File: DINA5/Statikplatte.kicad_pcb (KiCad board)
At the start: 2 copper layers, 100 x 100 mm, 32 parts, among them J1 VIN, J10 HV, J2 GND, J3 GND, J4 GND, J5 GND, J6 GND, J7 HV, J8 HV, J9 HV

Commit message: added DINA5 files
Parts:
- removed G***: LOGO, otter:otter_small1
- J1, J10, J2, J3, J4, J5, J6, J7, J8, J9: footprint TestPoint:TestPoint_Pad_2.5x2.5mm -> otter:Pads7.5x12
- moved J10 81.0 mm to (21.0, 104.0)
- moved J6 81.0 mm to (21.0, 74.0)
- moved J5 42.6 mm to (105.0, 21.0), turned to 270 degrees
- moved J8 42.6 mm to (135.0, 21.0), turned to 90 degrees
- moved J1 36.7 mm to (79.0, 83.0)
- moved J3 35.7 mm to (79.0, 95.0)
- moved C6 32.0 mm to (119.9, 95.0)
- moved C1 32.0 mm to (90.0, 83.0)
- moved C10 32.0 mm to (143.9, 95.0)
- moved C2 32.0 mm to (96.0, 95.0)
- moved C3 32.0 mm to (102.0, 83.0)
- moved C4 32.0 mm to (108.0, 95.0)
- moved C5 32.0 mm to (114.0, 83.0)
- moved C7 32.0 mm to (126.0, 83.0)
- moved C8 32.0 mm to (132.0, 95.0)
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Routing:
- net /GND: track 209.7 -> 312.2 mm
- net /HV: track 188.9 -> 267.2 mm
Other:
- board size 100 x 100 mm -> 210 x 148 mm

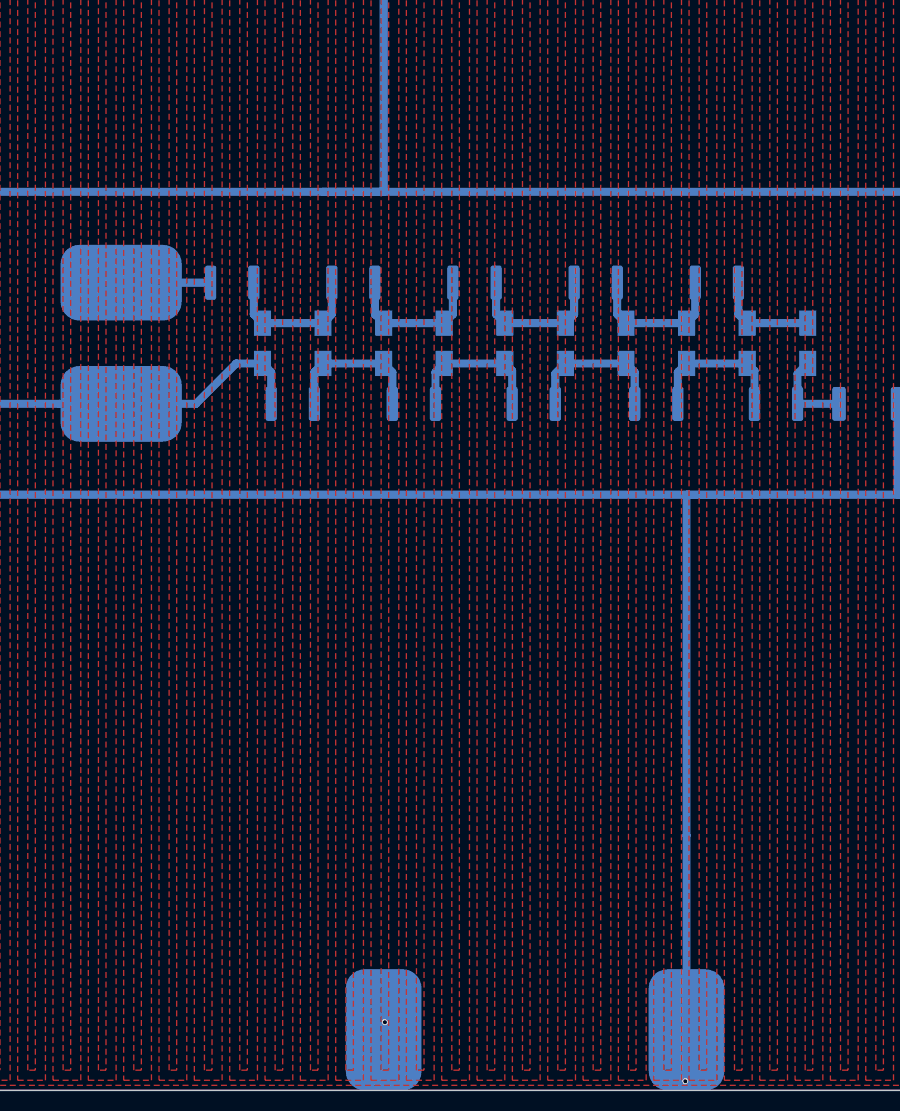
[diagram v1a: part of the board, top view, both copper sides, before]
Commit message: added screws
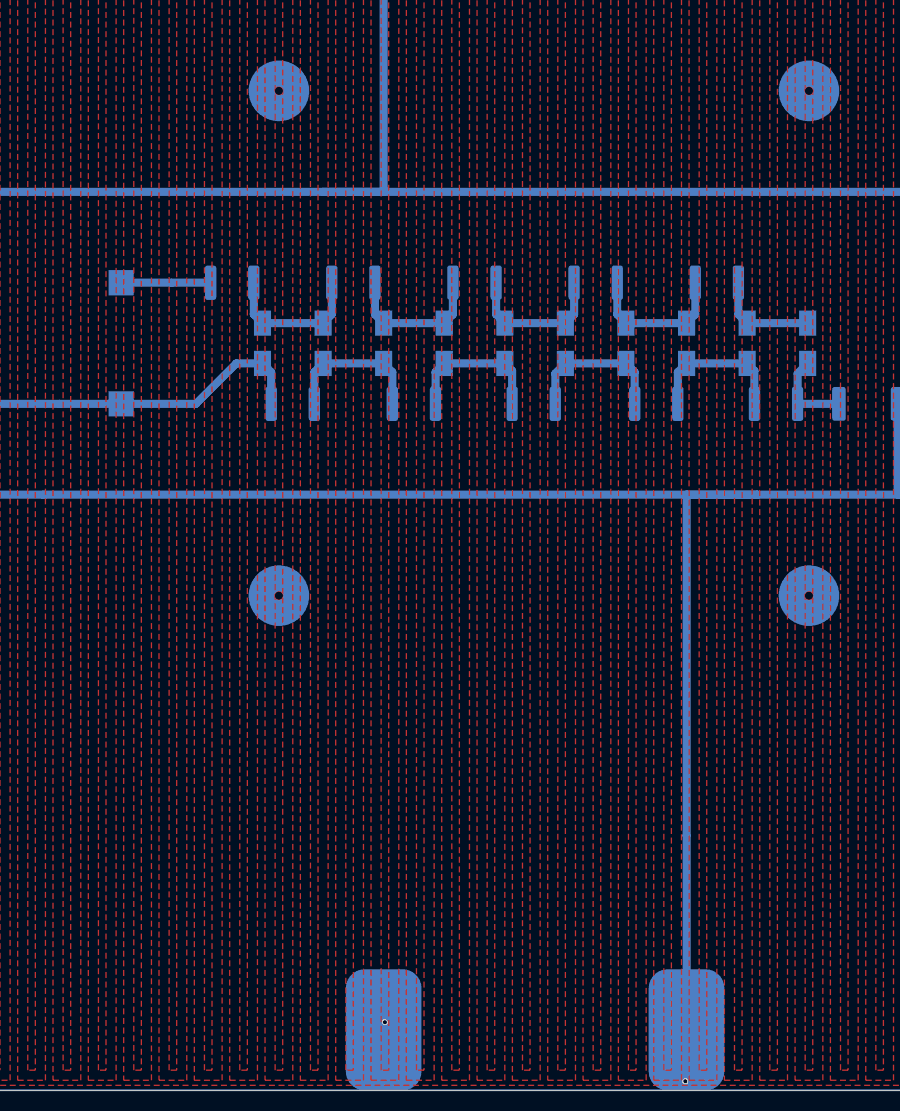
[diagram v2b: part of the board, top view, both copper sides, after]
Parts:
- added J11: SCREW, otter:M3_Screw, B.Cu at (147.1, 64.0)
- added J12: SCREW, otter:M3_Screw, B.Cu at (147.1, 114.0)
- added J13: SCREW, otter:M3_Screw, B.Cu at (94.6, 64.0)
- added J14: SCREW, otter:M3_Screw, B.Cu at (94.6, 114.0)
- J1, J3: footprint otter:Pads7.5x12 -> TestPoint:TestPoint_Pad_2.5x2.5mm
- J10, J2, J4, J5, J6, J7, J8, J9: footprint otter:Pads7.5x12 -> otter:PAD7.5x12
- turned J2 to 270 degrees
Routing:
- net Net-(C1-Pad2): track 3.86 -> 8.86 mm
